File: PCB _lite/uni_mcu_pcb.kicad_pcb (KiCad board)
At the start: 2 copper layers, 65 parts, among them J1 USB_C_Receptacle_USB2.0, J2 Conn_01x02_Male, J3 Conn_02x08_Odd_Even, Q1 Q_NPN_BCE, Q2 Q_NPN_BCE, Q3 Q_NPN_BCE, Q4 Q_NPN_BCE, Q5 FDS6890A, Q6 FDS6890A, SW1 SW_DIP_x01, SW2 SW_DIP_x01, SW3 SW_DIP_x01, U1 CC56-12CGKWA, U2 CH330N, U3 USBLC6-2P6, U4 STM32F030K6Tx, U5 LD1117S33TR_SOT223, U6 STM32F030C8Tx, U7 W25Q32JVSS, Y1 Crystal

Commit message: Добавлена lite версия платы
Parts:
- removed RN2: R_Pack05, Resistor_SMD:R_Array_Convex_5x0603
- removed SW3: SW_DIP_x01, Button_Switch_SMD:SW_Push_1P1T_NO_Vertical_Wuerth_434133025816
- removed U6: STM32F030C8Tx, Package_QFP:LQFP-48_7x7mm_P0.5mm
- added J4: Conn_01x05_Female, TerminalBlock_MetzConnect:TerminalBlock_MetzConnect_Type011_RT05505HBWC_1x05_P5.00mm_Horizontal, F.Cu at (170.0, 110.0)
- added R27: R, Resistor_SMD:R_0603_1608Metric_Pad0.98x0.95mm_HandSolder, F.Cu at (168.7, 118.8)
- added R28: R, Resistor_SMD:R_0603_1608Metric_Pad0.98x0.95mm_HandSolder, F.Cu at (173.0, 116.3)
- moved R16 75.1 mm to (168.7, 116.3), turned to 0 degrees
- moved R25 26.3 mm to (195.7, 103.7), turned to 0 degrees
- moved R26 25.5 mm to (195.7, 106.2), turned to 0 degrees
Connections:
- J3 pad 10: Net-(J3-Pad10) -> OUT3
- J3 pad 8: Net-(J3-Pad8) -> OUT4
- JP1 pad 1: USART1_TX -> a
- JP2 pad 1: USART1_RX -> b
- R16 pad 1: SW2 -> e_I2C1_SDA
- R18 pad 1: OUT4_CTRL -> CA4_CTRL
- R20 pad 1: OUT3_CTRL -> CA3_CTRL
- R22 pad 2: OUT4_CTRL -> CA4_CTRL
- R24 pad 2: OUT3_CTRL -> CA3_CTRL
- R25 pad 1: I2C1_SCL -> d_I2C1_SCL
- R25 pad 2: +3V3 -> unconnected-(R25-Pad2)
- R26 pad 1: I2C1_SDA -> d_I2C1_SCL
- R26 pad 2: +3V3 -> Net-(J3-Pad2)
- U1 pad 1: e -> e_I2C1_SDA
- U1 pad 2: d -> d_I2C1_SCL
- U4 pad 19: d -> d_I2C1_SCL
- U4 pad 20: e -> e_I2C1_SDA
- U4 pad 8: OUT1_CTRL -> OUT2_CTRL
- U4 pad 9: OUT2_CTRL -> OUT1_CTRL
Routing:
- net e_I2C1_SDA: track 0.00 -> 18.8 mm, vias 0 -> 2
- net e: track 18.8 -> 0.00 mm, vias 2 -> 0
- net d_I2C1_SCL: track 0.00 -> 17.9 mm, vias 0 -> 2
- net d: track 17.9 -> 0.00 mm, vias 2 -> 0

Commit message: Частично разведена плата
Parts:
- removed RN1: R_Pack05, Resistor_SMD:R_Array_Convex_5x0603
- removed U3: USBLC6-2P6, Package_TO_SOT_SMD:SOT-666
- removed U7: W25Q32JVSS, Package_SO:SOIC-8_5.23x5.23mm_P1.27mm
- added J5: Conn_01x04_Female, Connector_Hirose:Hirose_DF11-4DP-2DSA_2x02_P2.00mm_Vertical, B.Cu at (105.4, 135.4)
- added R29: R, Resistor_SMD:R_0603_1608Metric_Pad0.98x0.95mm_HandSolder, F.Cu at (102.4, 166.6)
- added R30: R, Resistor_SMD:R_0603_1608Metric_Pad0.98x0.95mm_HandSolder, F.Cu at (102.4, 163.8)
- added R31: R, Resistor_SMD:R_0603_1608Metric_Pad0.98x0.95mm_HandSolder, F.Cu at (102.4, 161.0)
- added R32: R, Resistor_SMD:R_0603_1608Metric_Pad0.98x0.95mm_HandSolder, F.Cu at (102.2, 158.0)
- C1, C10, C2, C6, C7, D2, D3, J1, Q1, Q2, Q3, Q4, R1, R11, R12, R16, R17, R18, R19, R2, R20, R27, R3, R4, R5, R6, R9, U2, U4, U5: moved to B.Cu
- J2: footprint Connector_PinHeader_2.54mm:PinHeader_1x02_P2.54mm_Vertical -> TerminalBlock_MetzConnect:TerminalBlock_MetzConnect_Type011_RT05502HBWC_1x02_P5.00mm_Horizontal
- moved R15 156.8 mm to (102.4, 169.4), turned to 0 degrees
- moved D1 141.1 mm to (106.4, 156.3), turned to 90 degrees
- moved R7 139.5 mm to (107.2, 151.2), turned to 90 degrees
- moved R10 138.8 mm to (104.1, 151.2), turned to 90 degrees
- moved J2 137.4 mm to (138.7, 168.4), turned to -90 degrees
- moved R8 133.7 mm to (110.0, 151.2), turned to 90 degrees
- moved R25 130.9 mm to (75.4, 155.5)
- moved R26 130.9 mm to (75.4, 158.0)
- moved R14 119.4 mm to (133.1, 153.2)
- moved D4 118.4 mm to (135.6, 161.8), turned to 180 degrees
- moved SW2 114.9 mm to (137.4, 148.6), turned to -90 degrees
- moved C10 114.4 mm to (145.5, 153.9), turned to 90 degrees
- moved D3 113.6 mm to (135.8, 156.5)
- moved Q6 105.2 mm to (114.2, 160.1), turned to -90 degrees
- moved R20 99.2 mm to (117.1, 154.0), turned to -90 degrees
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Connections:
- JP1 pad 1: a -> d
- JP2 pad 1: b -> c
- R15 pad 1: +3V3 -> Net-(J3-Pad1)
- R15 pad 2: Net-(R15-Pad2) -> PB0_IO
- U1 pad 1: e_I2C1_SDA -> e_I2C1_SCL
- U1 pad 11: a -> a_I2C1_SDA
- U1 pad 2: d_I2C1_SCL -> d
- U4 pad 12: a -> g
- U4 pad 13: b -> c
- U4 pad 18: c -> d
- U4 pad 19: d_I2C1_SCL -> e_I2C1_SCL
- U4 pad 20: e_I2C1_SDA -> a_I2C1_SDA
- U4 pad 22: g -> b
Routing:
- net GND: track 0.00 -> 95.1 mm
- net Net-(C9-Pad1): track 0.00 -> 78.6 mm
- net PB0_IO: track 0.00 -> 53.9 mm, vias 0 -> 2
- net SW1: track 0.00 -> 47.7 mm, vias 0 -> 1
- net SPI1_SCK: track 0.00 -> 45.7 mm, vias 0 -> 3
- net SPI1_MISO: track 0.00 -> 43.9 mm, vias 0 -> 3
- net CA3_CTRL: track 0.00 -> 38.1 mm, vias 0 -> 3
- net PB1_IO: track 0.00 -> 33.4 mm, vias 0 -> 1
- net CA1: track 0.00 -> 31.5 mm
- net Q2: track 0.00 -> 27.3 mm
- net Q1: track 0.00 -> 26.0 mm
- net OUT1_CTRL: track 0.00 -> 25.2 mm, vias 0 -> 3
- net CA4_CTRL: track 0.00 -> 23.9 mm, vias 0 -> 1
- net OUT2_CTRL: track 0.00 -> 23.9 mm, vias 0 -> 3
- net Net-(J3-Pad4): track 0.00 -> 23.8 mm, vias 0 -> 1
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
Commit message: разведена плата
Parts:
- C4, C5, C9: moved to B.Cu
- moved C9 102.1 mm to (129.3, 157.9)
- moved C8 89.0 mm to (119.0, 157.5), turned to 90 degrees
- moved R13 67.6 mm to (132.8, 156.3), turned to 180 degrees
- moved C3 51.0 mm to (108.7, 161.4)
- moved C5 34.6 mm to (132.5, 135.8), turned to 0 degrees
- moved R25 33.3 mm to (104.0, 172.6), turned to -90 degrees
- moved R26 29.7 mm to (101.3, 172.6), turned to -90 degrees
- moved C4 18.5 mm to (106.0, 128.4), turned to 0 degrees
- moved C10 16.3 mm to (129.3, 154.2)
- moved D4 5.04 mm to (139.4, 158.5)
- moved SW1 3.86 mm to (140.8, 153.4), turned to 0 degrees
- moved SW2 3.70 mm to (140.8, 147.2), turned to 180 degrees
- moved J2 3.11 mm to (138.3, 165.4)
- moved R14 1.27 mm to (134.4, 153.2)
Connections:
- R16 pad 1: e_I2C1_SDA -> a_I2C1_SDA
- R25 pad 1: d_I2C1_SCL -> e_I2C1_SCL
- R25 pad 2: unconnected-(R25-Pad2) -> +3V3
- R26 pad 1: d_I2C1_SCL -> e_I2C1_SCL
- R27 pad 1: e_I2C1_SDA -> a_I2C1_SDA
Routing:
- net GND: track 95.1 -> 362.5 mm, vias 0 -> 13
- net +3V3: track 6.30 -> 184.3 mm, vias 0 -> 11
- net OUT1: track 9.25 -> 79.3 mm
- net VCC: track 22.4 -> 81.0 mm, vias 1 -> 2
- net +5V: track 4.27 -> 53.0 mm, vias 0 -> 4
- net OUT2: track 9.74 -> 58.0 mm
- net RESET: track 7.68 -> 50.0 mm
- net e_I2C1_SCL: track 7.96 -> 48.1 mm, vias 0 -> 1
- net OUT3: track 9.27 -> 47.0 mm
- net OUT4: track 9.77 -> 43.1 mm
- net Net-(C9-Pad1): track 78.6 -> 111.7 mm
- net a_I2C1_SDA: track 12.6 -> 38.3 mm, vias 0 -> 2
- net c: track 12.1 -> 30.5 mm, vias 0 -> 1
- net Net-(J3-Pad6): track 0.00 -> 16.1 mm
- net SPI1_MOSI: track 22.2 -> 35.5 mm
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- added copper zone on B.Cu, net GND
- added copper zone on F.Cu, net GND
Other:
- board outline added: 60 x 60 mm

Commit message: Расставлены номиналы
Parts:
- moved U2 0.51 mm to (98.6, 128.3)
- moved R2 0.42 mm to (130.2, 132.3)
- moved R1 0.40 mm to (134.1, 132.3)
- moved R5 0.38 mm to (90.8, 129.2)
- moved J5 0.27 mm to (105.4, 135.6)
- moved J1 0.25 mm to (91.7, 137.2)
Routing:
- net GND: track 362.5 -> 348.3 mm, vias 13 -> 14
- net +3V3: track 184.3 -> 188.7 mm
- net /USB_D-: track 6.19 -> 3.46 mm
- net VCC: track 81.0 -> 79.6 mm
- net Net-(R9-Pad2): track 7.67 -> 8.26 mm
- net Net-(C2-Pad2): track 12.4 -> 11.8 mm
- net dpx_swdio: track 9.22 -> 9.79 mm
- net /USB_D+: track 6.57 -> 7.07 mm
- net c: track 30.5 -> 30.0 mm, vias 1 -> 0
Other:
- board size 60 x 60 mm -> 57 x 60 mm
- board text added: "+5V +3.3V OUT2 OUT3 OUT4 PA7 PA10 PA9"
- board text added: "GND"
- board text added: "GND VCC OUT1 PB5 PB4 PB3 PB1 PB0"
- board text added: "OUT4 OUT3 OUT2 OUT1 GND"
- board text added: "VCC"

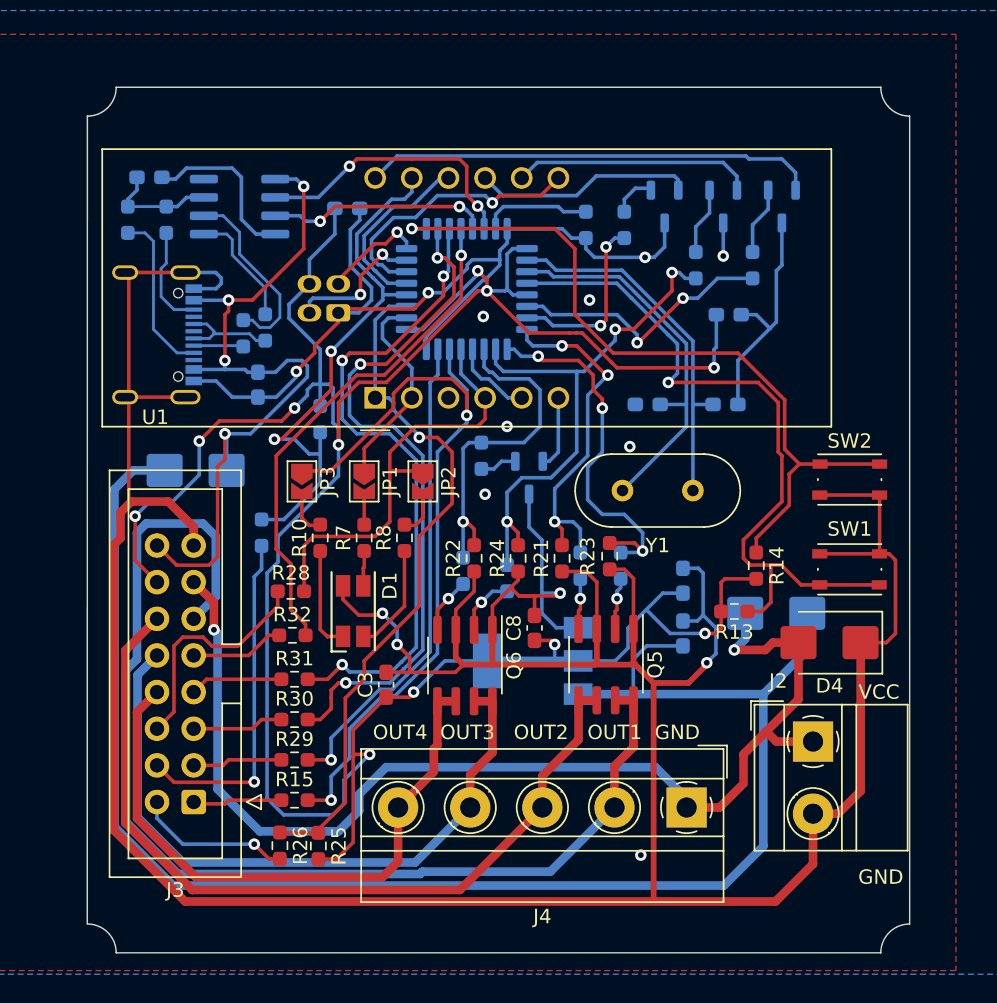
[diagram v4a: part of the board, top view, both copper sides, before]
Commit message: Отредактирована распиновка, доделана шелкография
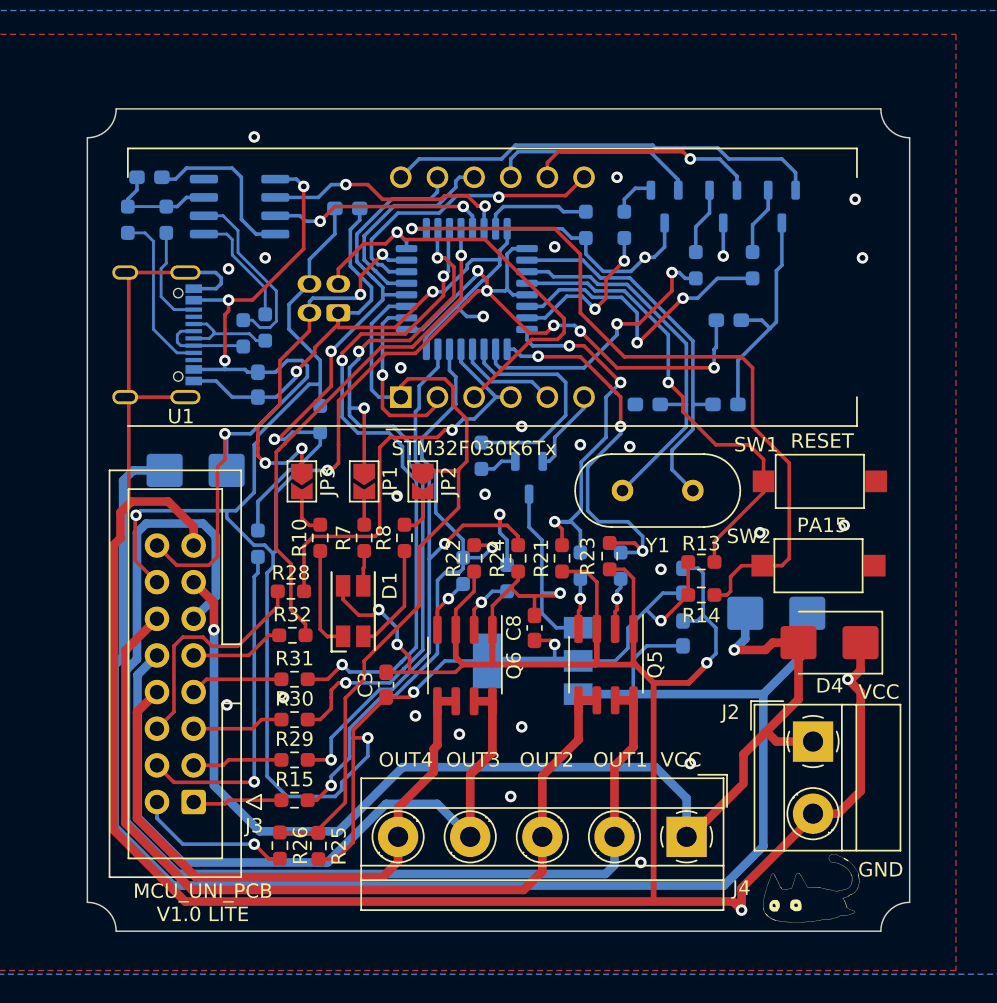
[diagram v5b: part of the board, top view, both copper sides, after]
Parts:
- added REF**: cat2, cat:cat2, F.Cu at (137.8, 180.7)
- added REF**: cat, cat:cat, B.Cu at (140.2, 142.0)
- C1, C10, C2, C3, C4, C5, C8: value C -> 0.1
- C6, C7: value C -> 22pF
- C9: value C -> 0.3
- D2: value DIODE -> SS24
- D3: value DIODE -> ss24
- D4: value D_TVS -> TVS24
- Q5, Q6: value FDS6890A -> F7313
- R1, R12, R13, R14, R2, R21, R22, R23, R24, R3, R4: value R -> 10K
- R10, R7, R8: value R -> 330
- R11, R15, R26, R27, R28, R29, R30, R31, R32, R9: value R -> 100
- R16, R25: value R -> 5.1K
- R17, R18, R19, R20, R5, R6: value R -> 1K
- SW1, SW2: footprint Button_Switch_SMD:SW_Push_1P1T_NO_Vertical_Wuerth_434133025816 -> Button_Switch_SMD:SW_SPST_CK_RS282G05A3
- Y1: value Crystal -> 8 Mhz
- moved SW1 6.44 mm to (138.8, 147.3), turned to 180 degrees
- moved SW2 6.35 mm to (138.7, 153.2)
- moved R14 4.32 mm to (130.6, 155.2), turned to 180 degrees
- moved R13 4.12 mm to (130.6, 152.9)
- moved J4 2.03 mm to (129.5, 172.0)
- moved U1 1.78 mm to (109.7, 141.5)
- moved R27 0.80 mm to (99.8, 151.6)
- moved C5 0.38 mm to (132.5, 136.1)
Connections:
- JP1 pad 1: d -> SPI1_SCK
- JP2 pad 1: c -> e_I2C1_SCL
- JP3 pad 1: PB0_IO -> dpx_swdio
- R18 pad 1: CA4_CTRL -> PB0_IO
- R20 pad 1: CA3_CTRL -> PB1_IO
- R22 pad 2: CA4_CTRL -> PB0_IO
- R24 pad 2: CA3_CTRL -> PB1_IO
- U1 pad 3: dpx -> swclk
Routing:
- net swclk: track 7.13 -> 30.7 mm
- net GND: track 348.3 -> 328.8 mm, vias 14 -> 35
- net CA3_CTRL: track 37.8 -> 19.1 mm, vias 3 -> 2
- net RESET: track 50.0 -> 32.5 mm
- net dpx_swdio: track 9.79 -> 26.4 mm, vias 2 -> 4
- net PB1_IO: track 33.7 -> 47.0 mm, vias 1 -> 3
- net PB0_IO: track 54.4 -> 43.2 mm
- net CA4_CTRL: track 23.9 -> 16.1 mm, vias 1 -> 0
- net e_I2C1_SCL: track 48.1 -> 55.3 mm, vias 1 -> 0
- net SPI1_SCK: track 48.2 -> 54.1 mm, vias 3 -> 4
- net +3V3: track 188.7 -> 183.1 mm
- net OUT3: track 47.0 -> 50.1 mm
- net /USB_D-: track 3.46 -> 6.44 mm
- net OUT2: track 58.0 -> 60.6 mm
- net OUT1: track 79.3 -> 81.7 mm
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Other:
- board size 57 x 60 mm -> 57 x 57 mm
- board text added: "MСU_UNI_PCB V1.0 LITE"
- board text added: "OUT4 OUT3 OUT2 OUT1 VCC"
- board text added: "PA15"
- board text added: "RESET"
- board text added: "STM32F030K6Tx"
- board text added: "VCC PA3 PA2 PB1 PB0"
- board text removed: "OUT4 OUT3 OUT2 OUT1 GND"

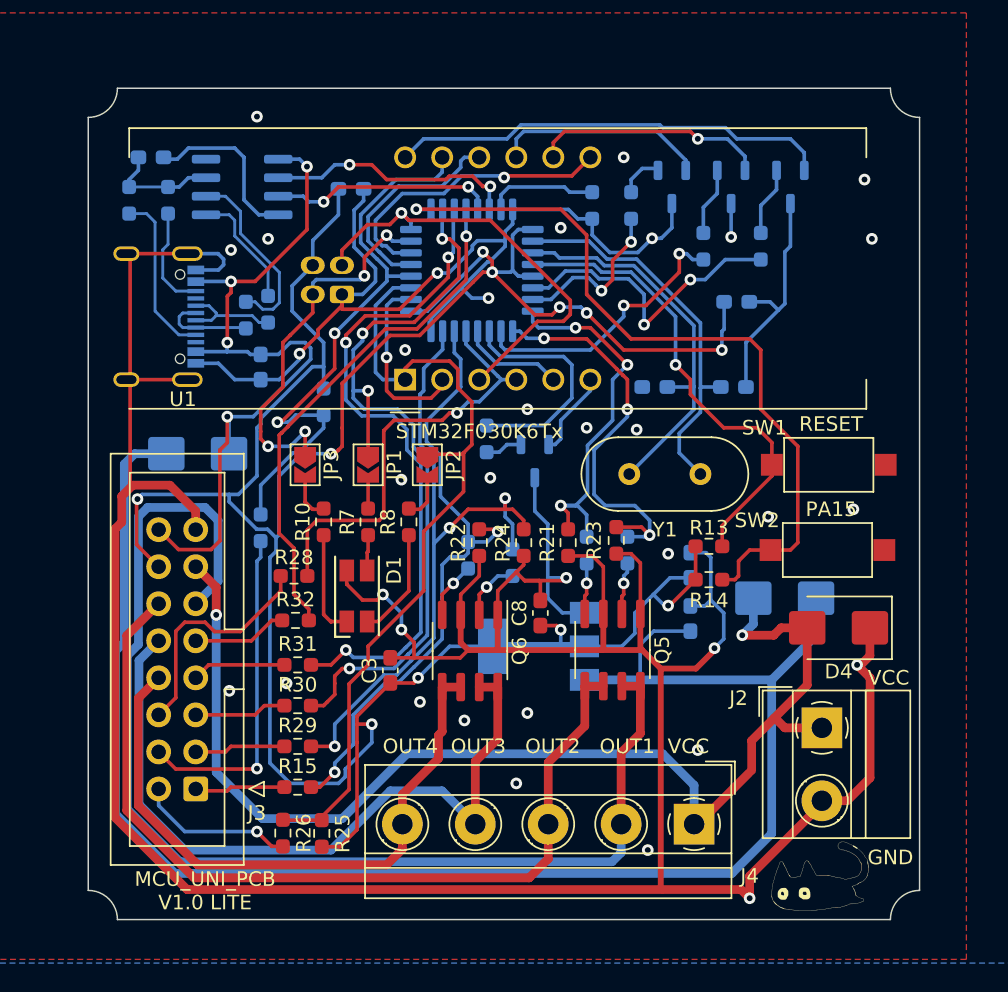
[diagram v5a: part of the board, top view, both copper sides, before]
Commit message: Схема теперь А4, Сформированы герберы
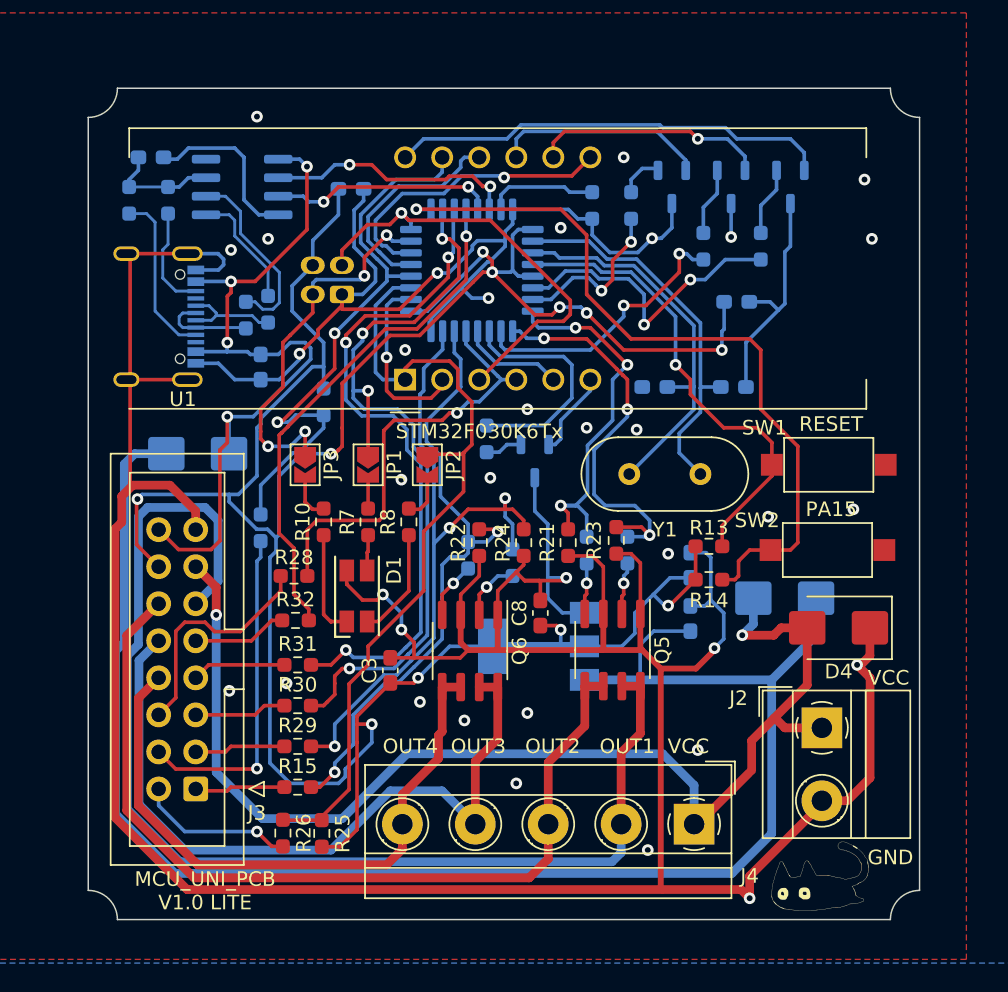
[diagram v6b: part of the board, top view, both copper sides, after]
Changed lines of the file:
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@@
       (outputformat 1)
       (mirror false)
-      (drillshape 1)
+      (drillshape 0)
       (scaleselection 1)
-      (outputdirectory "")
+      (outputdirectory "gerb_mcu_board/")
     )
   )
@@
     (fp_line (start 4.52 21.69) (end -1.98 21.69) (layer "F.Fab") (width 0.1))
     (fp_line (start -1.98 21.69) (end -1.98 10.94) (layer "F.Fab") (width 0.1))
-    (pad "1" thru_hole roundrect (at 0 0 180) (size 1.7 1.7) (drill 1) (layers *.Cu *.Mask) (roundrect_rratio 0.147059)
+    (pad "1" thru_hole roundrect (at 0 0 180) (size 1.7 1.7) (drill 1) (layers *.Cu *.Mask) (roundrect_rratio 0.1470588235)
       (net 57 "Net-(J3-Pad1)") (pinfunction "Pin_1") (pintype "passive"))
     (pad "2" thru_hole circle (at 2.54 0 180) (size 1.7 1.7) (drill 1) (layers *.Cu *.Mask)
@@
     (fp_line (start 4 -3.5) (end 4 1.5) (layer "B.Fab") (width 0.1))
     (fp_line (start 0 0.792893) (end 0.5 1.5) (layer "B.Fab") (width 0.1))
-    (pad "1" thru_hole roundrect locked (at 0 0 90) (size 1.2 1.65) (drill 0.85) (layers *.Cu *.Mask) (roundrect_rratio 0.208333)
+    (pad "1" thru_hole roundrect locked (at 0 0 90) (size 1.2 1.65) (drill 0.85) (layers *.Cu *.Mask) (roundrect_rratio 0.2083333333)
       (net 1 "GND") (pinfunction "Pin_1") (pintype "passive"))
     (pad "2" thru_hole oval locked (at 0 -2 90) (size 1.2 1.65) (drill 0.85) (layers *.Cu *.Mask)
@@
     )
   )
-  (gr_arc (start 143 178.5) (mid 143.585786 177.085787) (end 145 176.5) (layer "Edge.Cuts") (width 0.1))
-  (gr_arc (start 145 123.5) (mid 143.585787 122.914214) (end 143 121.5) (layer "Edge.Cuts") (width 0.1))
-  (gr_arc (start 90 121.5) (mid 89.414214 122.914213) (end 88 123.5) (layer "Edge.Cuts") (width 0.1))
+  (gr_arc (start 143 178.5) (mid 143.585786 177.085786) (end 145 176.5) (layer "Edge.Cuts") (width 0.1))
+  (gr_arc (start 145 123.5) (mid 143.585786 122.914214) (end 143 121.5) (layer "Edge.Cuts") (width 0.1))
+  (gr_arc (start 90 121.5) (mid 89.414214 122.914214) (end 88 123.5) (layer "Edge.Cuts") (width 0.1))
   (gr_line (start 143 121.5) (end 90 121.5) (layer "Edge.Cuts") (width 0.1))
   (gr_line (start 145 176.5) (end 145 123.5) (layer "Edge.Cuts") (width 0.1))
-  (gr_arc (start 88 176.5) (mid 89.414213 177.085786) (end 90 178.5) (layer "Edge.Cuts") (width 0.1))
+  (gr_arc (start 88 176.5) (mid 89.414214 177.085786) (end 90 178.5) (layer "Edge.Cuts") (width 0.1))
   (gr_line (start 90 178.5) (end 143 178.5) (layer "Edge.Cuts") (width 0.1))
   (gr_line (start 88 123.5) (end 88 176.5) (layer "Edge.Cuts") (width 0.1))
